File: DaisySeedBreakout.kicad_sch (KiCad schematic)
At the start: 47 parts, among them J2 Conn_01x02, J24 Conn_01x02, J25 Conn_01x02, J26 Conn_02x04, J30 Conn_01x02, J31 Conn_02x04, J32 Conn_01x02, J33 Conn_01x02, J34 Conn_01x02, J35 Conn_01x02, J6 Conn_01x02, U10 TPD2EUSB30ADRTR, U11 TPS560200DBVR

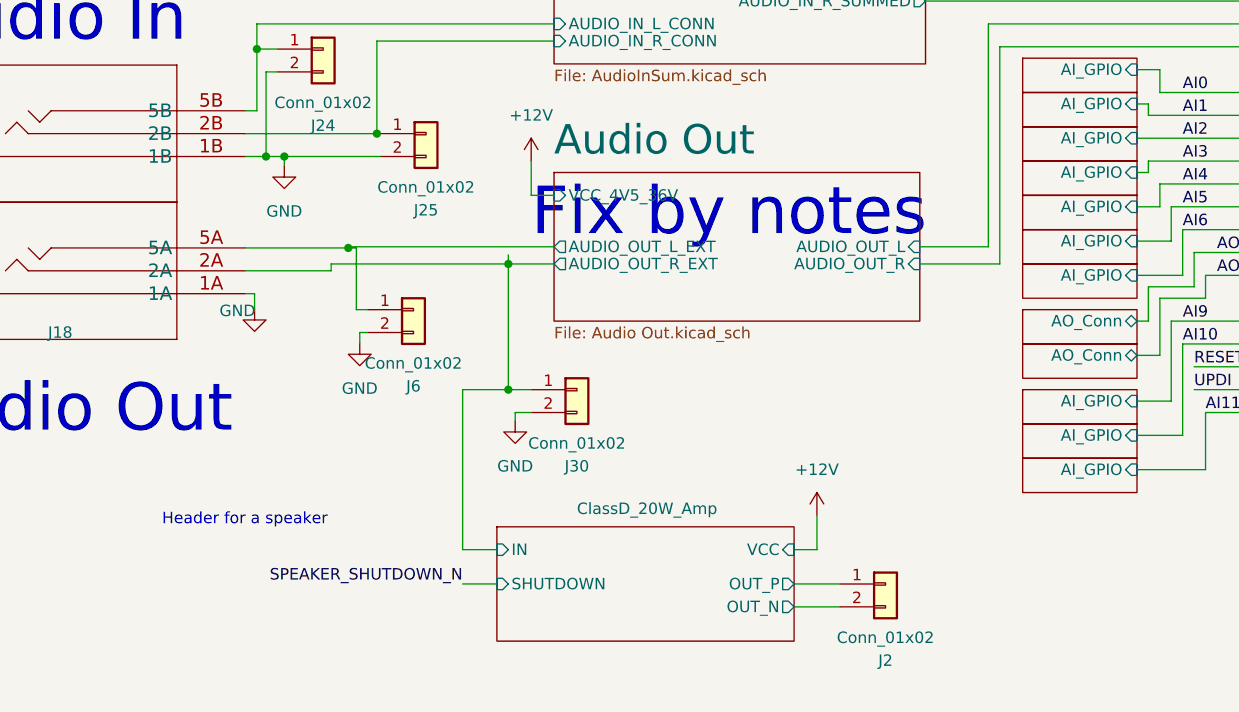
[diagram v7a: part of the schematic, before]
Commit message: Update Audio out to switch between 1V ptp or 10V ptp based on jumper
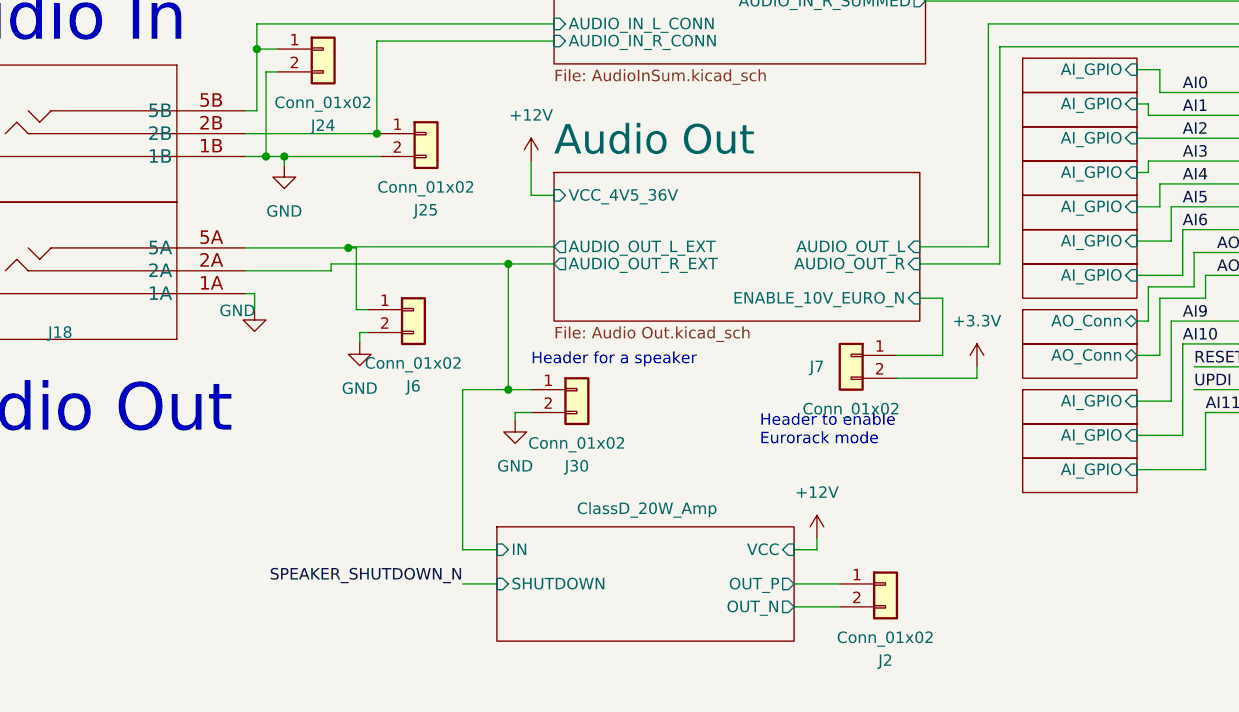
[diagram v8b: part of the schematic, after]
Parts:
- added J7: Conn_01x02, Connector_PinHeader_2.54mm:PinHeader_1x02_P2.54mm_Vertical, symbol 4ms_Connector:Conn_01x02
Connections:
- net +3.3V: now also J7.2 (Pin_2)
- new net Audio Out/ENABLE_10V_EURO_N: J7.1 (Pin_1)
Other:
- sheet Audio Out ports: added ENABLE_10V_EURO_N; removed none
- note added: "Header to enable Eurorack mode"
- note removed: "Fix by notes"
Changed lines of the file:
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@@
     (stroke (width 0) (type default))
   )
+  (wire (pts (xy 137.16 116.84) (xy 128.27 116.84))
+    (stroke (width 0) (type default))
+  )
   (wire (pts (xy 154.94 86.36) (xy 156.21 86.36))
     (stroke (width 0) (type default))
@@
     (stroke (width 0) (type default))
   )
-  (wire (pts (xy 85.09 103.124) (xy 85.09 104.14))
-    (stroke (width 0) (type default))
-  )
   (wire (pts (xy 139.7 185.42) (xy 139.7 189.23))
     (stroke (width 0) (type default))
@@
     (stroke (width 0) (type default))
   )
+  (wire (pts (xy 133.35 107.95) (xy 130.81 107.95))
+    (stroke (width 0) (type default))
+  )
   (wire (pts (xy 99.06 189.23) (xy 95.25 189.23))
     (stroke (width 0) (type default))
@@
     (stroke (width 0) (type default))
   )
+  (wire (pts (xy 137.16 115.57) (xy 137.16 116.84))
+    (stroke (width 0) (type default))
+  )
   (wire (pts (xy 353.06 68.58) (xy 365.76 68.58))
     (stroke (width 0) (type default))
@@
     (stroke (width 0) (type default))
   )
-  (wire (pts (xy 119.38 135.89) (xy 119.38 132.08))
+  (wire (pts (xy 119.38 135.89) (xy 119.38 134.62))
     (stroke (width 0) (type default))
   )
@@
     (stroke (width 0) (type default))
   )
+  (wire (pts (xy 128.27 114.3) (xy 133.35 114.3))
+    (stroke (width 0) (type default))
+  )
   (wire (pts (xy 250.19 57.15) (xy 262.89 57.15))
     (stroke (width 0) (type default))
@@
     (stroke (width 0) (type default))
   )
+  (wire (pts (xy 133.35 114.3) (xy 133.35 107.95))
+    (stroke (width 0) (type default))
+  )
   (wire (pts (xy 294.64 254) (xy 294.64 255.27))
     (stroke (width 0) (type default))
@@
     (effects (font (size 5.27 5.27)) (justify left bottom))
   )
+  (text "Header to enable\nEurorack mode" (at 113.03 124.46 0)
+    (effects (font (size 1.27 1.27)) (justify left bottom))
+  )
   (text "1.16V Threshold\n7V Max allowed" (at 184.15 260.35 0)
     (effects (font (size 1.27 1.27)) (justify left bottom))
@@
     (effects (font (size 5.27 5.27)) (justify left bottom))
   )
-  (text "Header for a speaker" (at 46.609 133.35 0)
+  (text "Header for a speaker" (at 87.63 115.57 0)
     (effects (font (size 1.27 1.27)) (justify left bottom))
   )
@@
     (effects (font (size 5.27 5.27)) (justify left bottom))
   )
-  (text "Fix by notes" (at 87.63 101.6 0)
-    (effects (font (size 5.27 5.27)) (justify left bottom))
-  )
   (label "AI2" (at 160.02 90.17 0) (fields_autoplaced)
     (effects (font (size 1.27 1.27)) (justify left bottom))
@@
     )
   )
+  (symbol (lib_id "power:+3.3V") (at 137.16 115.57 0) (unit 1)
+    (in_bom yes) (on_board yes) (dnp no) (fields_autoplaced)
+    (property "Reference" "#PWR0174" (at 137.16 119.38 0)
+      (effects (font (size 1.27 1.27)) hide)
+    )
+    (property "Value" "+3.3V" (at 137.16 110.49 0)
+      (effects (font (size 1.27 1.27)))
+    )
+    (property "Footprint" "" (at 137.16 115.57 0)
+      (effects (font (size 1.27 1.27)) hide)
+    )
+    (property "Datasheet" "" (at 137.16 115.57 0)
+      (effects (font (size 1.27 1.27)) hide)
+    )
+    (pin "1")
+    (instances
+      (project "DaisySeedBreakout"
+        (path "/a83c9f4b-f61b-47d4-b39d-4636bff6eb0e"
+          (reference "#PWR0174") (unit 1)
+        )
+      )
+    )
+  )
   (symbol (lib_id "4ms_Connector:Conn_02x04") (at 87.63 184.15 0) (unit 1)
     (in_bom yes) (on_board yes) (dnp no) (fields_autoplaced)
@@
     )
   )
-  (symbol (lib_id "4ms_Power-symbol:+12V") (at 119.38 132.08 0) (unit 1)
+  (symbol (lib_id "4ms_Power-symbol:+12V") (at 119.38 134.62 0) (unit 1)
     (in_bom yes) (on_board yes) (dnp no) (fields_autoplaced)
-    (property "Reference" "#PWR0135" (at 119.38 135.89 0)
+    (property "Reference" "#PWR0135" (at 119.38 138.43 0)
       (effects (font (size 1.27 1.27)) hide)
     )
-    (property "Value" "+12V" (at 119.38 127 0)
+    (property "Value" "+12V" (at 119.38 129.54 0)
       (effects (font (size 1.27 1.27)))
     )
-    (property "Footprint" "" (at 119.38 132.08 0)
+    (property "Footprint" "" (at 119.38 134.62 0)
       (effects (font (size 1.27 1.27)) hide)
     )
-    (property "Datasheet" "" (at 119.38 132.08 0)
+    (property "Datasheet" "" (at 119.38 134.62 0)
       (effects (font (size 1.27 1.27)) hide)
     )
@@
     )
   )
+  (symbol (lib_id "4ms_Connector:Conn_01x02") (at 123.19 114.3 0) (mirror y) (unit 1)
+    (in_bom yes) (on_board yes) (dnp no)
+    (property "Reference" "J7" (at 119.38 115.57 0)
+      (effects (font (size 1.27 1.27)))
+    )
+    (property "Value" "Conn_01x02" (at 123.19 120.269 0)
+      (effects (font (size 1.27 1.27)))
+    )
+    (property "Footprint" "Connector_PinHeader_2.54mm:PinHeader_1x02_P2.54mm_Vertical" (at 123.825 109.855 0)
+      (effects (font (size 1.27 1.27)) hide)
+    )
+    (property "Datasheet" "" (at 123.19 114.3 0)
+      (effects (font (size 1.27 1.27)) hide)
+    )
+    (property "Specifications" "Pins_01x02, Header, Male Pins, 1*2, spacing 2.54mm, straight pin" (at 125.73 122.174 0)
+      (effects (font (size 1.27 1.27)) (justify left) hide)
+    )
+    (property "Manufacturer" "TAD" (at 125.73 123.698 0)
+      (effects (font (size 1.27 1.27)) (justify left) hide)
+    )
+    (property "Part Number" "1-0201FBV0T" (at 125.73 125.222 0)
+      (effects (font (size 1.27 1.27)) (justify left) hide)
+    )
+    (pin "1")
+    (pin "2")
+    (instances
+      (project "DaisySeedBreakout"
+        (path "/a83c9f4b-f61b-47d4-b39d-4636bff6eb0e"
+          (reference "J7") (unit 1)
+        )
+      )
+    )
+  )
   (symbol (lib_id "4ms_Connector:Conn_01x02") (at 363.22 187.96 0) (unit 1)
     (in_bom yes) (on_board yes) (dnp no) (fields_autoplaced)
@@
       (effects (font (size 1.27 1.27)) (justify right))
     )
+    (pin "ENABLE_10V_EURO_N" input (at 130.81 107.95 0)
+      (effects (font (size 1.27 1.27)) (justify right))
+    )
